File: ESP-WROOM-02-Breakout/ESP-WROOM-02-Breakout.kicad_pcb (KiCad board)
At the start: 2 copper layers, 59.4 x 16.3 mm, 10 parts, among them IC1 ESP-WROOM-02U__4MB_, J1 Left Pins, J2 Right Pins, J3 UART

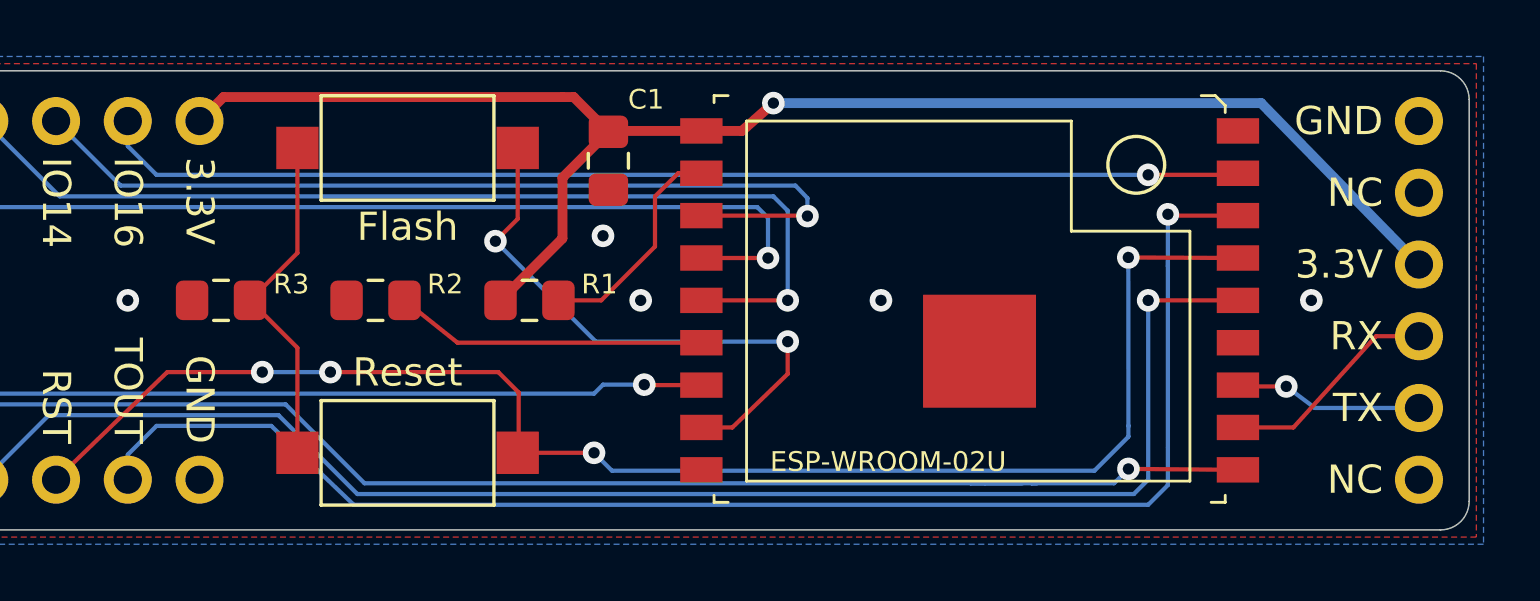
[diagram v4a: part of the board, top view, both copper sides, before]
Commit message: add voltage/current/wifi info on silkscreen
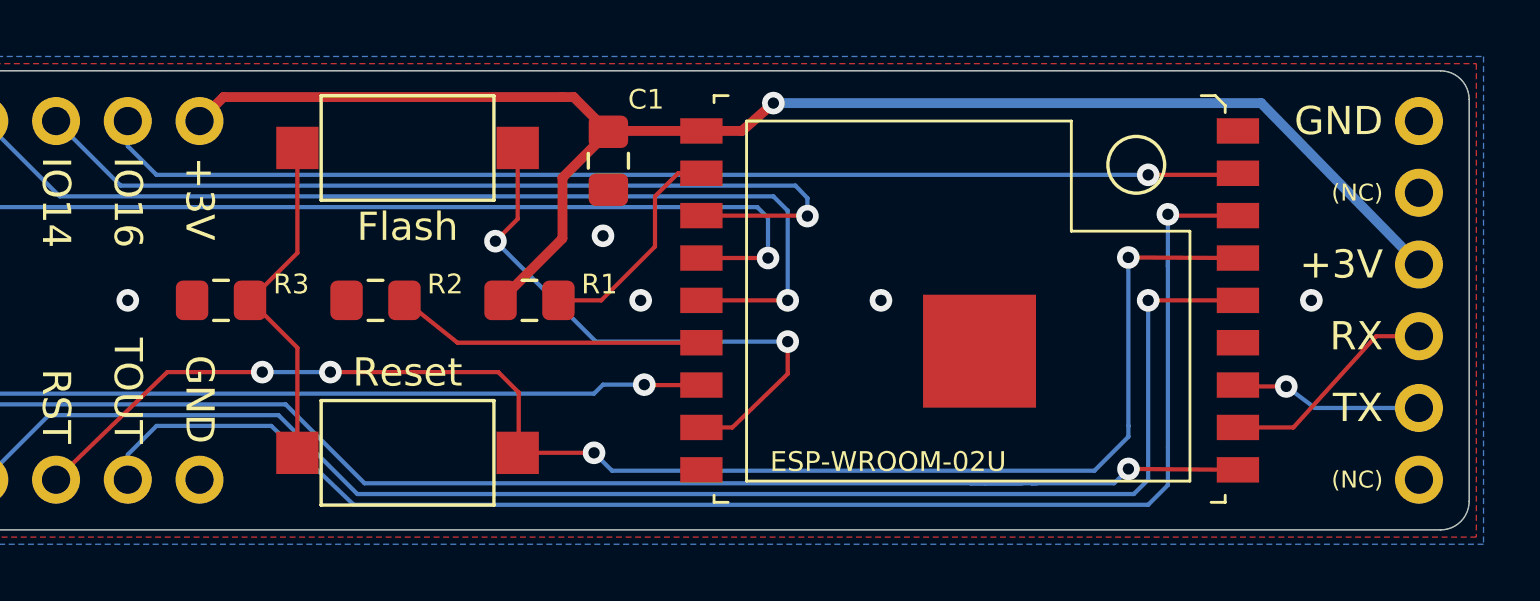
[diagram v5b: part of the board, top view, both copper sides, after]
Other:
- board text added: "(NC)"
- board text added: "+3V"
- board text added: "2.7-3.6V @ max 500mA 802.11 b/g/n 2.4GHz"
- board text removed: "3.3V"
- board text removed: "NC"
